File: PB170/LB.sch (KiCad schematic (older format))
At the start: 6 parts

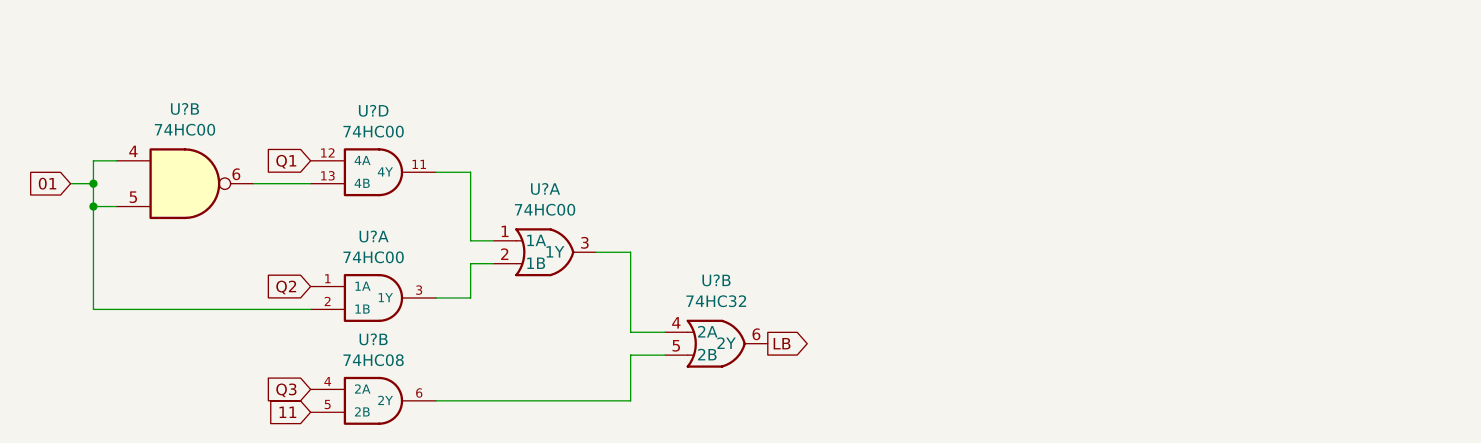
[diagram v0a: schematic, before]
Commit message: added LEDs, mby we could try to start routing
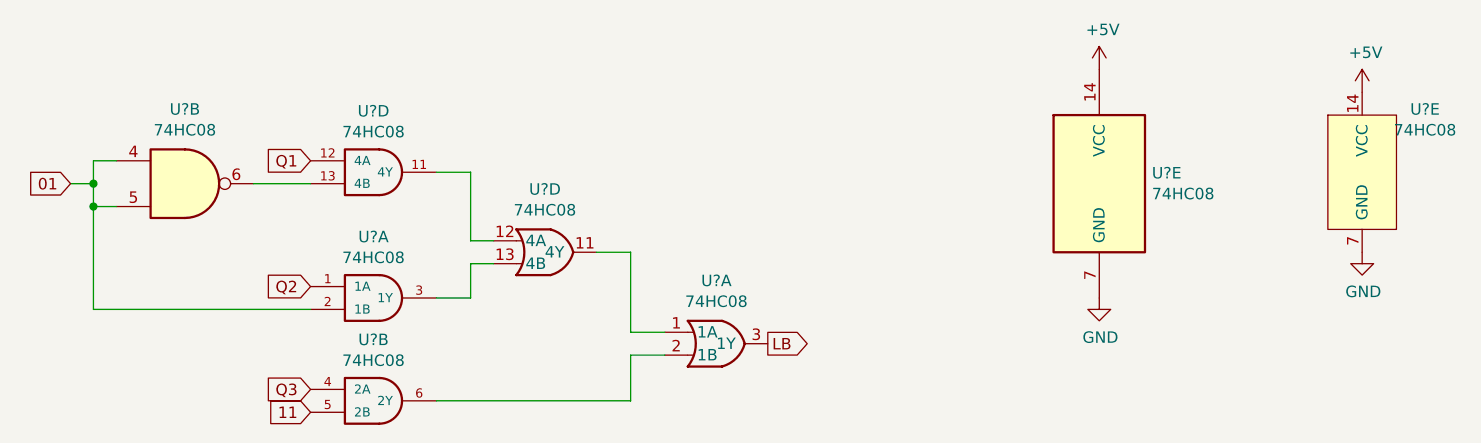
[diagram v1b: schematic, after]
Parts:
- added U?: 74HC08, Housings_SOIC:SOIC-14_3.9x8.7mm_Pitch1.27mm, symbol PB170:74HC08
- added U?: 74HC08, Housings_SOIC:SOIC-14_3.9x8.7mm_Pitch1.27mm, symbol PB170:74HC32
- U? (x4): value 74HC00 -> 74HC08; footprint Package_SO:TSSOP-14_4.4x5mm_P0.65mm -> Housings_SOIC:SOIC-14_3.9x8.7mm_Pitch1.27mm
- U?: value 74HC32 -> 74HC08
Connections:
- net LB: now also U?.3 (1Y); no longer U?.6 (2Y)
- net at U?.11 (4Y): now also U?.12 (4A); no longer U?.1 (1A)
- net at U?.3 (1Y): now also U?.13 (4B); no longer U?.2 (1B)
- net at U?.6 (2Y): now also U?.2 (1B); no longer U?.5 (2B)
- new net: U?.1 (1A), U?.11 (4Y)
- new net +5V: U?.14 (VCC), U?.14 (VCC)
- new net GND: U?.7 (GND), U?.7 (GND)
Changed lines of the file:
@@
 $Comp
 L PB170:74HC32 U?
-U 1 1 60274CEA
+U 4 1 60274CEA
 P 6150 3150
 F 0 "U?" H 6125 3425 50  0000 C CNN
-F 1 "74HC00" H 6125 3334 50  0000 C CNN
-F 2 "Package_SO:TSSOP-14_4.4x5mm_P0.65mm" H 5600 3350 50  0001 C CNN
-F 3 "https://datasheet.lcsc.com/szlcsc/Texas-Instruments-TI-SN74HC00PWR_C6807.pdf" H 5600 3350 50  0001 C CNN
+F 1 "74HC08" H 6125 3334 50  0000 C CNN
+F 2 "Housings_SOIC:SOIC-14_3.9x8.7mm_Pitch1.27mm" H 5600 3350 50  0001 C CNN
+F 3 "https://datasheet.lcsc.com/szlcsc/Nexperia-74HC08D-653_C5593.pdf" H 5600 3350 50  0001 C CNN
 F 4 "C5632" H 6150 3150 50  0001 C CNN "LCSC"
-	1    6150 3150
+	4    6150 3150
 	1    0    0    -1
 $EndComp
 $Comp
 L PB170:74HC32 U?
-U 2 1 60275657
+U 1 1 60275657
 P 6900 3550
 F 0 "U?" H 6875 3825 50  0000 C CNN
-F 1 "74HC32" H 6875 3734 50  0000 C CNN
+F 1 "74HC08" H 6875 3734 50  0000 C CNN
 F 2 "Housings_SOIC:SOIC-14_3.9x8.7mm_Pitch1.27mm" H 6350 3750 50  0001 C CNN
-F 3 "https://datasheet.lcsc.com/szlcsc/Nexperia-74HC32D-653_C5632.pdf" H 6350 3750 50  0001 C CNN
+F 3 "https://datasheet.lcsc.com/szlcsc/Nexperia-74HC08D-653_C5593.pdf" H 6350 3750 50  0001 C CNN
 F 4 "C5632" H 6900 3550 50  0001 C CNN "LCSC"
-	2    6900 3550
+	1    6900 3550
 	1    0    0    -1
 $EndComp
@@
 P 5350 2800
 F 0 "U?" H 5375 3067 50  0000 C CNN
-F 1 "74HC00" H 5375 2976 50  0000 C CNN
-F 2 "Package_SO:TSSOP-14_4.4x5mm_P0.65mm" H 5350 2800 50  0001 C CNN
-F 3 "https://datasheet.lcsc.com/szlcsc/Texas-Instruments-TI-SN74HC00PWR_C6807.pdf" H 5350 2800 50  0001 C CNN
+F 1 "74HC08" H 5375 2976 50  0000 C CNN
+F 2 "Housings_SOIC:SOIC-14_3.9x8.7mm_Pitch1.27mm" H 5350 2800 50  0001 C CNN
+F 3 "https://datasheet.lcsc.com/szlcsc/Nexperia-74HC08D-653_C5593.pdf" H 5350 2800 50  0001 C CNN
 F 4 "C5593" H 5350 2800 50  0001 C CNN "LCSC"
 	4    5350 2800
@@
 P 5350 3350
 F 0 "U?" H 5375 3617 50  0000 C CNN
-F 1 "74HC00" H 5375 3526 50  0000 C CNN
-F 2 "Package_SO:TSSOP-14_4.4x5mm_P0.65mm" H 5350 3350 50  0001 C CNN
-F 3 "https://datasheet.lcsc.com/szlcsc/Texas-Instruments-TI-SN74HC00PWR_C6807.pdf" H 5350 3350 50  0001 C CNN
+F 1 "74HC08" H 5375 3526 50  0000 C CNN
+F 2 "Housings_SOIC:SOIC-14_3.9x8.7mm_Pitch1.27mm" H 5350 3350 50  0001 C CNN
+F 3 "https://datasheet.lcsc.com/szlcsc/Nexperia-74HC08D-653_C5593.pdf" H 5350 3350 50  0001 C CNN
 F 4 "C5593" H 5350 3350 50  0001 C CNN "LCSC"
 	1    5350 3350
@@
 AR Path="/6026DE84/60274732" Ref="U?"  Part="2"
 F 0 "U?" H 4550 3175 50  0000 C CNN
-F 1 "74HC00" H 4550 3084 50  0000 C CNN
-F 2 "Package_SO:TSSOP-14_4.4x5mm_P0.65mm" H 4550 2850 50  0001 C CNN
-F 3 "https://datasheet.lcsc.com/szlcsc/Texas-Instruments-TI-SN74HC00PWR_C6807.pdf" H 4550 2850 50  0001 C CNN
+F 1 "74HC08" H 4550 3084 50  0000 C CNN
+F 2 "Housings_SOIC:SOIC-14_3.9x8.7mm_Pitch1.27mm" H 4550 2850 50  0001 C CNN
+F 3 "https://datasheet.lcsc.com/szlcsc/Nexperia-74HC08D-653_C5593.pdf" H 4550 2850 50  0001 C CNN
 F 4 "C6807" H 4550 2850 50  0001 C CNN "LCSC"
 	2    4550 2850
@@
 Text GLabel 5100 3850 0    50   Input ~ 0
 11
+$Comp
+L PB170:74HC08 U?
+U 5 1 60275189
+P 8550 2850
+AR Path="/6026D736/60275189" Ref="U?"  Part="5"
+AR Path="/6026DE84/60275189" Ref="U?"  Part="5"
+F 0 "U?" H 8780 2896 50  0000 L CNN
+F 1 "74HC08" H 8780 2805 50  0000 L CNN
+F 2 "Housings_SOIC:SOIC-14_3.9x8.7mm_Pitch1.27mm" H 8550 2850 50  0001 C CNN
+F 3 "https://datasheet.lcsc.com/szlcsc/Nexperia-74HC08D-653_C5593.pdf" H 8550 2850 50  0001 C CNN
+F 4 "C5593" H 8550 2850 50  0001 C CNN "LCSC"
+	5    8550 2850
+	1    0    0    -1
+$EndComp
+$Comp
+L power:GND #PWR?
+U 1 1 6027518F
+P 8550 3350
+AR Path="/6026D736/6027518F" Ref="#PWR?"  Part="1"
+AR Path="/6026DE84/6027518F" Ref="#PWR?"  Part="1"
+F 0 "#PWR?" H 8550 3100 50  0001 C CNN
+F 1 "GND" H 8555 3177 50  0000 C CNN
+F 2 "" H 8550 3350 50  0001 C CNN
+F 3 "" H 8550 3350 50  0001 C CNN
+	1    8550 3350
+	1    0    0    -1
+$EndComp
+$Comp
+L power:+5V #PWR?
+U 1 1 60275195
+P 8550 2350
+AR Path="/6026D736/60275195" Ref="#PWR?"  Part="1"
+AR Path="/6026DE84/60275195" Ref="#PWR?"  Part="1"
+F 0 "#PWR?" H 8550 2200 50  0001 C CNN
+F 1 "+5V" H 8565 2523 50  0000 C CNN
+F 2 "" H 8550 2350 50  0001 C CNN
+F 3 "" H 8550 2350 50  0001 C CNN
+	1    8550 2350
+	1    0    0    -1
+$EndComp
+$Comp
+L power:GND #PWR?
+U 1 1 602B0446
+P 9700 3150
+AR Path="/6026D736/602B0446" Ref="#PWR?"  Part="1"
+AR Path="/6026DE84/602B0446" Ref="#PWR?"  Part="1"
+F 0 "#PWR?" H 9700 2900 50  0001 C CNN
+F 1 "GND" H 9705 2977 50  0000 C CNN
+F 2 "" H 9700 3150 50  0001 C CNN
+F 3 "" H 9700 3150 50  0001 C CNN
+	1    9700 3150
+	1    0    0    -1
+$EndComp
+$Comp
+L PB170:74HC32 U?
+U 5 1 602B044D
+P 10000 2800
+AR Path="/6026D736/602B044D" Ref="U?"  Part="5"
+AR Path="/6026DE84/602B044D" Ref="U?"  Part="5"
+F 0 "U?" H 9975 3075 50  0000 C CNN
+F 1 "74HC08" H 9975 2984 50  0000 C CNN
+F 2 "Housings_SOIC:SOIC-14_3.9x8.7mm_Pitch1.27mm" H 9450 3000 50  0001 C CNN
+F 3 "https://datasheet.lcsc.com/szlcsc/Nexperia-74HC08D-653_C5593.pdf" H 9450 3000 50  0001 C CNN
+F 4 "C5632" H 10000 2800 50  0001 C CNN "LCSC"
+	5    10000 2800
+	1    0    0    -1
+$EndComp
+$Comp
+L power:+5V #PWR?
+U 1 1 602B0453
+P 9700 2450
+AR Path="/6026D736/602B0453" Ref="#PWR?"  Part="1"
+AR Path="/6026DE84/602B0453" Ref="#PWR?"  Part="1"
+F 0 "#PWR?" H 9700 2300 50  0001 C CNN
+F 1 "+5V" H 9715 2623 50  0000 C CNN
+F 2 "" H 9700 2450 50  0001 C CNN
+F 3 "" H 9700 2450 50  0001 C CNN
+	1    9700 2450
+	1    0    0    -1
+$EndComp
 $EndSCHEMATC
